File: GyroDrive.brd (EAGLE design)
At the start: 8.1 x 9.3 mm, 32 parts

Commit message: Preliminary board layout
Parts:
- moved ICOM 65.9 mm to (11.6, 11.2)
- moved GND 55.3 mm to (1.04, 14.4)
- moved IX 54.6 mm to (11.0, 3.02)
- moved STIM1OUT 49.8 mm to (1.21, 12.4)
- moved MOTORGND 49.3 mm to (11.2, 0.83)
- moved STIM1IN 44.4 mm to (2.78, 10.1)
- moved REF 44.1 mm to (7.25, 18.9)
- moved U$10 40.8 mm to (4.70, 10.6)
- moved E4 36.6 mm to (5.55, 18.9)
- moved E5 35.1 mm to (3.23, 14.6)
- moved E3 32.8 mm to (3.78, 19.2)
- moved E2 26.5 mm to (3.20, 16.2)
- moved E1 24.5 mm to (2.95, 17.8)
- moved U$8 21.0 mm to (1.05, 19.7), turned to 180 degrees
- moved U$7 20.1 mm to (1.54, 19.4), turned to 180 degrees
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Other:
- board size 8.1 x 9.3 mm -> 8.1 x 21 mm

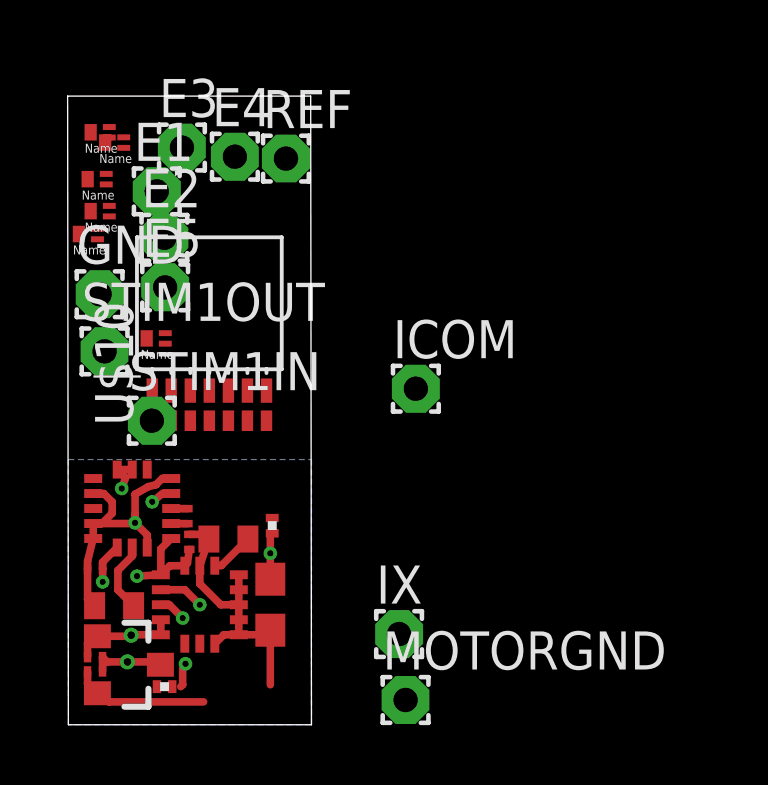
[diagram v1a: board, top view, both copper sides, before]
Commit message: Preliminary layout with smaller through-holes
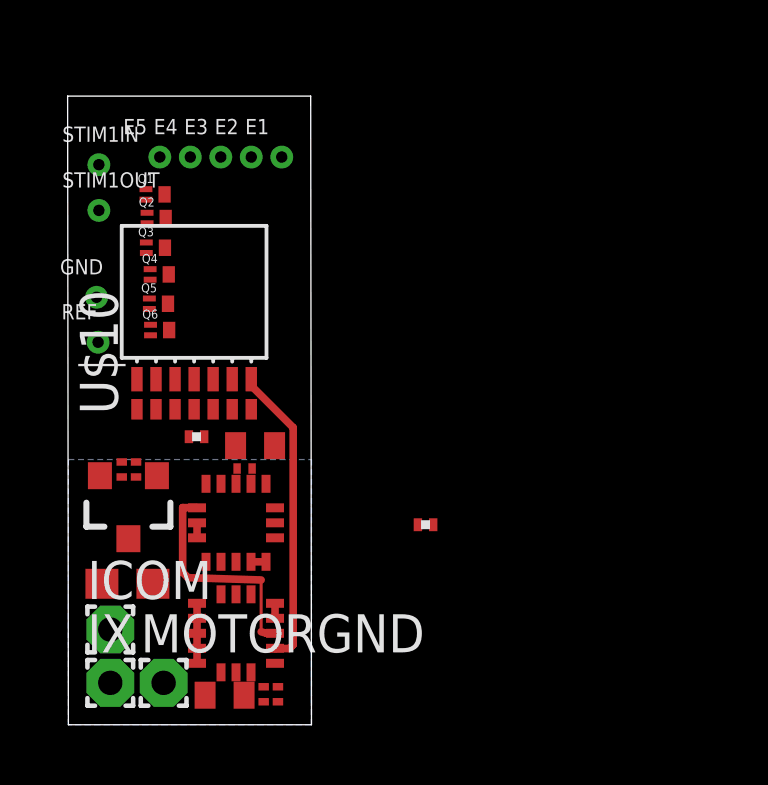
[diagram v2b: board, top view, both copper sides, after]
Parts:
- removed U$4, U$5, U$6, U$7, U$8, U$9: TF412ST5G, on-semiconductor-mes:SOT883
- added Q1, Q2, Q3, Q4, Q5, Q6: TF412ST5G, on-semiconductor-mes:SOT883
- E1, E2, E3, E4, E5, GND, REF, STIM1IN, STIM1OUT: device wirepad:1,6/0,8 -> michael-stetner:30MIL/15MIL
- moved ICOM 13.0 mm to (1.40, 3.17)
- moved IX 9.76 mm to (1.40, 1.40)
- moved REF 8.76 mm to (0.99, 12.8)
- moved STIM1IN 8.72 mm to (1.02, 18.7)
- moved R2 8.40 mm to (4.27, 9.60)
- moved MOTORGND 8.08 mm to (3.17, 1.40)
- moved C3 7.40 mm to (6.99, 1.02), turned to 270 degrees
- moved C8 7.11 mm to (6.22, 9.30)
- moved C1 6.79 mm to (1.78, 8.51), turned to 270 degrees
- moved C2 6.40 mm to (2.25, 8.51), turned to 270 degrees
- moved C4 5.65 mm to (6.51, 1.02), turned to 270 degrees
- moved U$2 5.30 mm to (2.00, 7.30), turned to 180 degrees
- moved C7 5.21 mm to (5.21, 0.98)
- moved R1 5.11 mm to (11.9, 6.67), turned to 0 degrees
- moved C5 4.81 mm to (1.97, 4.70), turned to 180 degrees
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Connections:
- net +15V: now also Q1.P$2, Q2.P$2, Q3.P$2, Q4.P$2, Q5.P$2, Q6.P$2; no longer U$4.P$2, U$5.P$2, U$6.P$2, U$7.P$2, U$8.P$2, U$9.P$2
- net GND: now also GND.P$1; no longer GND.1
- net N$10: now also E1.P$1, Q1.P$3; no longer E1.1, U$4.P$3
- net N$11: now also STIM1OUT.P$1; no longer STIM1OUT.1
- net N$16: now also STIM1IN.P$1; no longer STIM1IN.1
- net N$4: now also Q6.P$3, REF.P$1; no longer REF.1, U$9.P$3
- net N$5: now also E5.P$1, Q5.P$3; no longer E5.1, U$8.P$3
- net N$6: now also E4.P$1, Q4.P$3; no longer E4.1, U$7.P$3
- net N$7: now also E3.P$1, Q3.P$3; no longer E3.1, U$6.P$3
- net N$8: now also E2.P$1, Q2.P$3; no longer E2.1, U$5.P$3
- net S1: now also Q1.P$1; no longer U$4.P$1
- net S2: now also Q2.P$1; no longer U$5.P$1
- net S3: now also Q3.P$1; no longer U$6.P$1
- net S4: now also Q4.P$1; no longer U$7.P$1
- net S5: now also Q5.P$1; no longer U$8.P$1
- net VGND: now also Q6.P$1; no longer U$9.P$1
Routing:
- net GND: track 22.3 -> 2.50 mm, vias 2 -> 0
- net +3V3: track 12.3 -> 1.59 mm, vias 5 -> 0
- net SCL: track 14.9 -> 22.2 mm, vias 3 -> 0
- net SDA: track 4.12 -> 10.7 mm, vias 1 -> 0
- net +15V: track 4.50 -> 0.00 mm
- net N$1: track 2.35 -> 0.00 mm
- net N$9: track 1.49 -> 0.00 mm
- net N$3: track 0.54 -> 0.00 mm
- net N$2: track 0.54 -> 0.00 mm

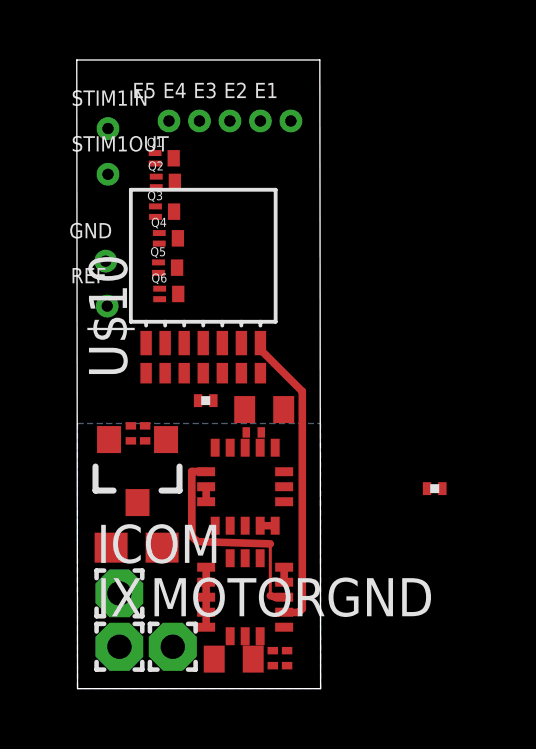
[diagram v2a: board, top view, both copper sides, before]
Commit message: Routing in progress. Having trouble with getting electrodes to FETs
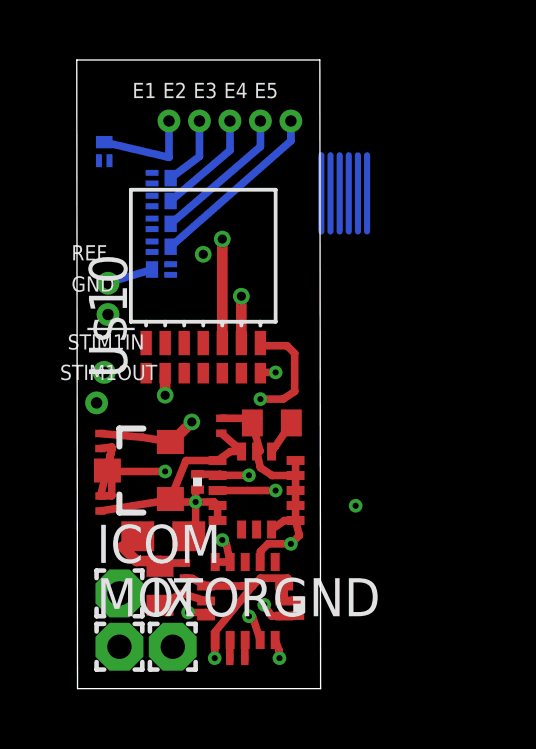
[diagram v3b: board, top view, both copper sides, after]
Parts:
- moved STIM1IN 8.13 mm to (0.89, 10.5)
- moved C7 7.98 mm to (6.48, 8.86)
- moved C4 7.93 mm to (4.79, 8.76), turned to 90 degrees
- moved R1 7.91 mm to (4.00, 6.89), turned to 270 degrees
- moved STIM1OUT 7.63 mm to (0.64, 9.53)
- moved C9 7.60 mm to (5.33, 0.96), turned to 180 degrees
- moved R2 7.56 mm to (7.34, 2.69), turned to 90 degrees
- moved C8 6.82 mm to (2.75, 3.43), turned to 90 degrees
- moved C3 4.49 mm to (3.58, 3.94), turned to 90 degrees
- moved E1 4.06 mm to (3.05, 18.9)
- moved E5 4.06 mm to (7.11, 18.9)
- moved U$3 3.81 mm to (5.59, 2.92), turned to 90 degrees
- moved U$1 3.58 mm to (5.97, 6.60), turned to 0 degrees
- moved C2 2.77 mm to (0.77, 6.17), turned to 90 degrees
- moved E2 2.03 mm to (4.06, 18.9)
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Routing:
- net GND: track 2.50 -> 33.6 mm, vias 0 -> 6
- net +3V3: track 1.59 -> 18.1 mm, vias 0 -> 2
- net N$12: track 0.00 -> 11.8 mm, vias 0 -> 1
- net N$15: track 0.00 -> 10.1 mm, vias 0 -> 1
- net SCL: track 22.2 -> 14.0 mm, vias 0 -> 3
- net N$5: track 0.00 -> 6.00 mm
- net +15V: track 0.00 -> 5.89 mm, vias 0 -> 2
- net N$6: track 0.00 -> 4.80 mm
- net N$7: track 0.00 -> 3.58 mm
- net N$10: track 0.00 -> 3.43 mm
- net N$21: track 0.00 -> 2.54 mm
- net N$20: track 0.00 -> 2.54 mm
- net N$19: track 0.00 -> 2.54 mm
- net N$18: track 0.00 -> 2.54 mm
- net N$17: track 0.00 -> 2.54 mm
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- added copper zone on layer 2, net +15V
- added copper zone on layer 3, net GND
- added copper zone on layer 3, net N$13
- removed copper zone on layer 16, net GND

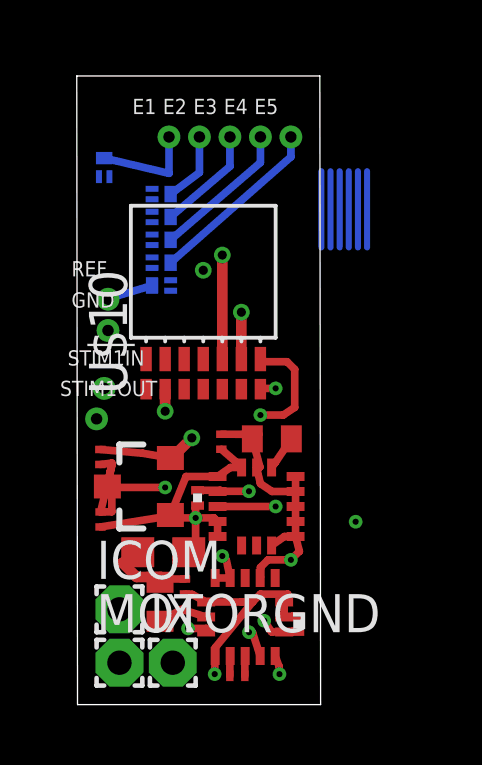
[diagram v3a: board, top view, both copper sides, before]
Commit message: Routing in progress. FETs done, except VGND. Still need to rout stim and motor.
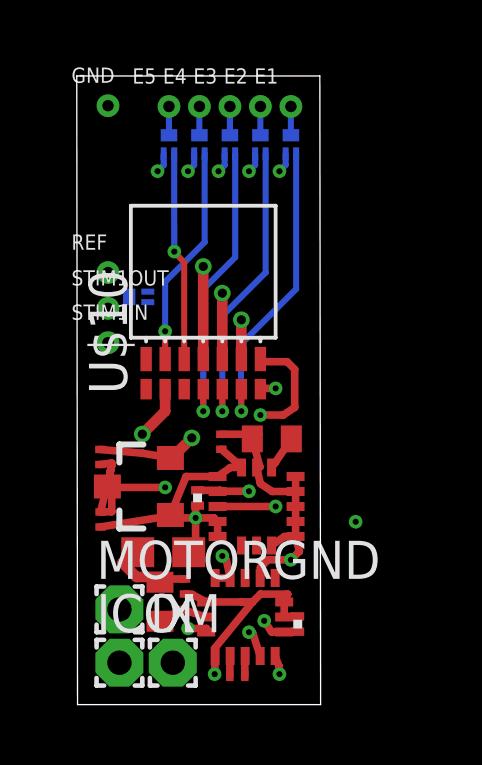
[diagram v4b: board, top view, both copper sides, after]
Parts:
- moved GND 7.49 mm to (1.02, 20.0)
- moved Q1 6.27 mm to (7.11, 18.7)
- moved E1 4.19 mm to (7.11, 19.9)
- moved E5 4.19 mm to (3.05, 19.9)
- moved Q5 3.95 mm to (3.05, 18.7), turned to 90 degrees
- moved STIM1OUT 3.70 mm to (1.02, 13.2)
- moved Q2 3.69 mm to (6.10, 18.7), turned to 90 degrees
- moved Q4 3.42 mm to (4.06, 18.7), turned to 90 degrees
- moved Q3 3.32 mm to (5.08, 18.7), turned to 90 degrees
- moved E2 2.27 mm to (6.10, 19.9)
- moved E4 2.27 mm to (4.06, 19.9)
- moved ICOM 1.78 mm to (1.40, 1.40)
- moved MOTORGND 1.78 mm to (1.40, 3.17)
- moved STIM1IN 1.53 mm to (1.02, 12.1)
- moved E3 1.02 mm to (5.08, 19.9)
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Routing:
- net S1: track 0.00 -> 10.3 mm, vias 0 -> 1
- net S2: track 0.00 -> 9.92 mm, vias 0 -> 1
- net S3: track 0.00 -> 9.76 mm, vias 0 -> 1
- net S4: track 0.00 -> 7.39 mm, vias 0 -> 1
- net S5: track 0.00 -> 6.97 mm, vias 0 -> 1
- net N$5: track 6.00 -> 0.96 mm
- net N$6: track 4.80 -> 0.96 mm
- net +15V: track 5.89 -> 8.96 mm, vias 2 -> 7
- net N$7: track 3.58 -> 0.96 mm
- net N$21: track 2.54 -> 0.00 mm
- net N$20: track 2.54 -> 0.00 mm
- net N$19: track 2.54 -> 0.00 mm
- net N$18: track 2.54 -> 0.00 mm
- net N$17: track 2.54 -> 0.00 mm
- net N$14: track 2.54 -> 0.00 mm
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- removed copper zone on layer 3, net N$13

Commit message: Routing done
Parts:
- moved Q6 1.78 mm to (2.16, 15.4), turned to 90 degrees
- moved REF 1.27 mm to (1.02, 15.7)
- moved STIM1IN 0.89 mm to (1.02, 13.0)
- moved STIM1OUT 0.89 mm to (1.02, 14.1)
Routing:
- net N$12: track 9.59 -> 17.4 mm
- net VGND: track 0.00 -> 6.52 mm, vias 0 -> 1
- net GND: track 35.0 -> 39.8 mm
- net N$16: track 0.00 -> 3.43 mm
- net N$11: track 0.00 -> 3.10 mm
- net N$4: track 0.00 -> 1.15 mm
- net +15V: track 8.96 -> 9.75 mm, vias 7 -> 8
- net SDA: track 11.2 -> 12.0 mm, vias 4 -> 3

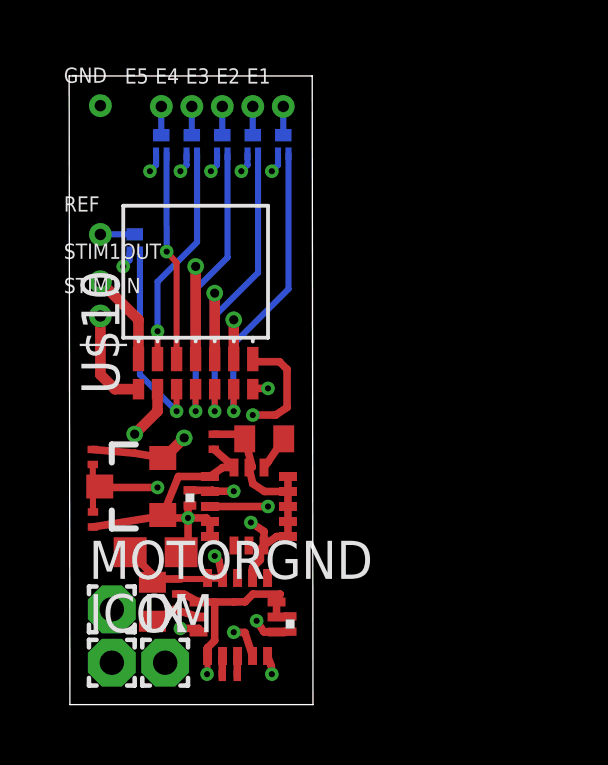
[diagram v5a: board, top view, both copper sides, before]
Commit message: In progress - rearrangement to put Omnetics connector lower, per Michale's suggestion
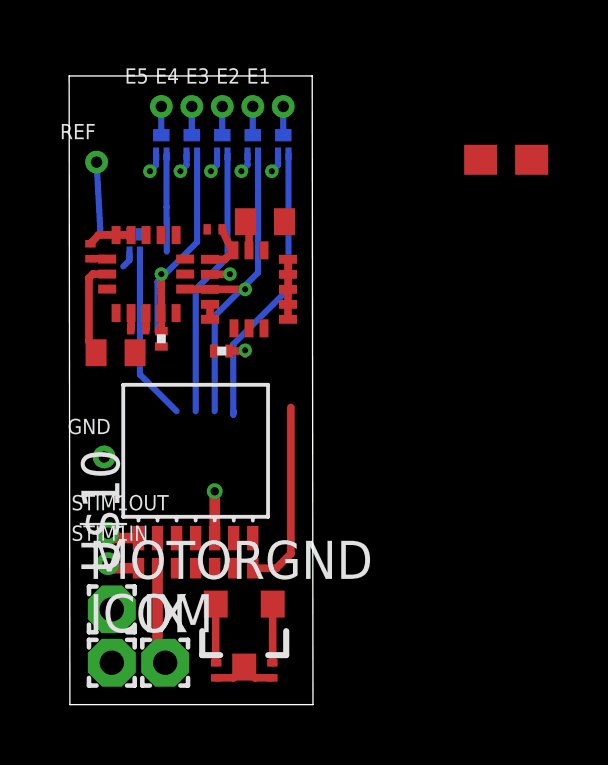
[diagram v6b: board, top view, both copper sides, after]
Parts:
- moved C5 17.5 mm to (14.5, 18.2)
- moved C9 12.0 mm to (2.28, 12.5)
- moved U$3 11.8 mm to (2.54, 14.4)
- moved GND 11.7 mm to (1.14, 8.26)
- moved C3 11.5 mm to (0.69, 15.1)
- moved R2 9.38 mm to (5.06, 11.8), turned to 180 degrees
- moved C8 8.39 mm to (1.52, 11.7), turned to 0 degrees
- moved STIM1OUT 8.39 mm to (1.27, 5.71)
- moved STIM1IN 8.26 mm to (1.27, 4.70)
- moved C1 8.22 mm to (4.88, 1.14)
- moved C2 7.81 mm to (6.75, 1.14), turned to 270 degrees
- moved C7 7.24 mm to (6.50, 16.1)
- moved U$1 7.24 mm to (5.97, 13.8)
- moved C4 7.08 mm to (4.83, 15.8), turned to 180 degrees
- moved U$2 6.17 mm to (5.81, 2.35), turned to 180 degrees
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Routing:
- net GND: track 39.8 -> 6.82 mm, vias 6 -> 0
- net +3V3: track 18.2 -> 4.76 mm, vias 2 -> 0
- net SCL: track 14.2 -> 4.86 mm, vias 3 -> 2
- net N$12: track 17.4 -> 8.48 mm
- net N$15: track 10.1 -> 3.25 mm, vias 1 -> 0
- net S5: track 6.97 -> 3.26 mm, vias 1 -> 0
- net +15V: track 9.75 -> 6.46 mm, vias 8 -> 5
- net N$4: track 1.15 -> 3.55 mm
- net N$16: track 3.43 -> 1.08 mm
- net N$11: track 3.10 -> 1.08 mm
- net N$1: track 1.68 -> 3.22 mm
- net N$9: track 1.16 -> 0.00 mm
- net SDA: track 12.0 -> 11.0 mm, vias 3 -> 2
- net S4: track 7.39 -> 6.46 mm, vias 1 -> 0
- net VGND: track 6.52 -> 5.78 mm, vias 1 -> 0
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- removed copper zone on layer 2, net +15V
- removed copper zone on layer 2, net +3V3
- removed copper zone on layer 3, net GND

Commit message: Routing finished
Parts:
- moved C5 11.8 mm to (4.89, 11.3), turned to 0 degrees
- moved Q6 3.36 mm to (1.52, 18.7)
- moved R2 2.16 mm to (7.21, 11.6), turned to 90 degrees
- moved C1 2.12 mm to (6.99, 0.94), turned to 0 degrees
- moved REF 1.96 mm to (1.52, 19.9)
- moved C2 1.69 mm to (6.99, 2.81), turned to 0 degrees
- moved U$2 0.48 mm to (5.78, 1.87), turned to 270 degrees
- moved C4 0.45 mm to (5.18, 16.1), turned to 90 degrees
- moved R1 0.28 mm to (3.30, 12.3), turned to 0 degrees
- moved C8 0.25 mm to (1.52, 11.5)
- moved C9 0.25 mm to (2.28, 12.3)
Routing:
- net GND: track 6.82 -> 40.8 mm, vias 0 -> 7
- net +15V: track 6.46 -> 31.0 mm, vias 5 -> 9
- net +3V3: track 4.76 -> 24.3 mm, vias 0 -> 5
- net SCL: track 4.86 -> 18.4 mm
- net VGND: track 5.78 -> 16.3 mm, vias 0 -> 1
- net S5: track 3.26 -> 13.3 mm, vias 0 -> 1
- net S4: track 6.46 -> 14.0 mm, vias 0 -> 1
- net S3: track 9.02 -> 16.3 mm, vias 0 -> 1
- net S2: track 9.18 -> 16.1 mm, vias 0 -> 1
- net S1: track 9.57 -> 16.1 mm, vias 0 -> 1
- net SDA: track 11.0 -> 14.2 mm
- net N$4: track 3.55 -> 0.96 mm
- net N$12: track 8.48 -> 9.81 mm
- net N$9: track 0.00 -> 1.24 mm
- added copper zone on layer 2, net +15V
- added copper zone on layer 2, net +3V3
- added copper zone on layer 3, net GND

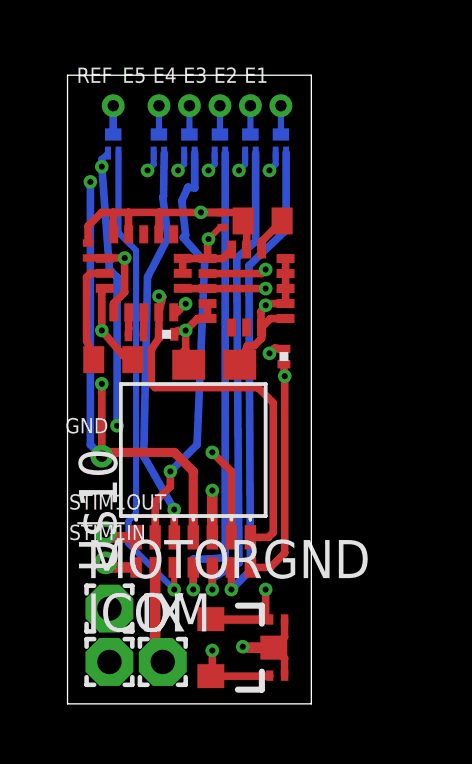
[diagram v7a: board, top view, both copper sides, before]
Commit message: Cleaned up routing
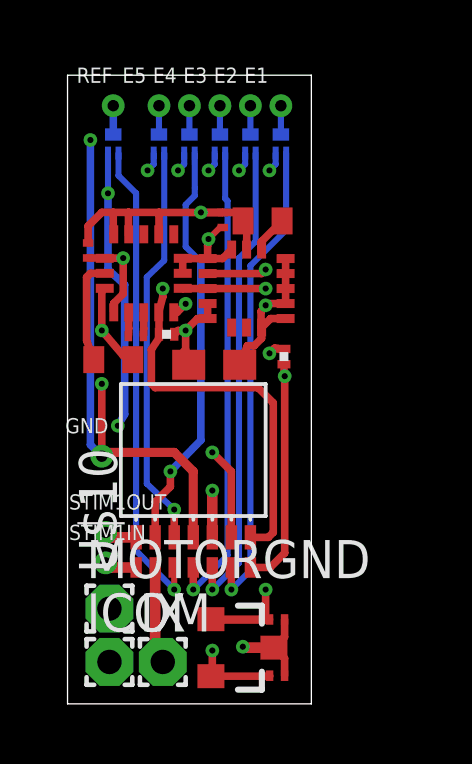
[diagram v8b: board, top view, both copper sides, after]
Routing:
- net GND: track 40.8 -> 42.1 mm
- net S3: track 16.3 -> 15.8 mm
